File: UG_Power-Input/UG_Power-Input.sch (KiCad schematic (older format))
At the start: 45 parts, among them J1 INPUT, J2 OUTPUT, J3 OUTPUT, U1 LM2679

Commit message: Changes to PCB design
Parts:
- removed H3: 3.5mm, MountingHole:MountingHole_3.5mm, symbol Mechanical:MountingHole
- added H3: 3.5mm, MountingHole:MountingHole_3.5mm_Pad_Via, symbol Mechanical:MountingHole_Pad
- added R3: 0Ω, Resistor_THT:R_Axial_DIN0207_L6.3mm_D2.5mm_P10.16mm_Horizontal, symbol Device:R
- L2, L4: Manufacturer (none) -> Coilcraft
- R2: footprint Resistor_THT:R_Axial_DIN0207_L6.3mm_D2.5mm_P2.54mm_Vertical -> Resistor_THT:R_Axial_DIN0207_L6.3mm_D2.5mm_P10.16mm_Horizontal
- renumbered TP11 to TP10, TP10 to TP11
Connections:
- net -IN: now reaches FL1.2, J1.2 (Pin_2), TP4.1
- net -IN: now also R3.1
- new net: H3.1, R3.2
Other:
- moved on the sheet: C1, C10, C11, C12, C13, C2, C3, C4, C5, C6, C7, C8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

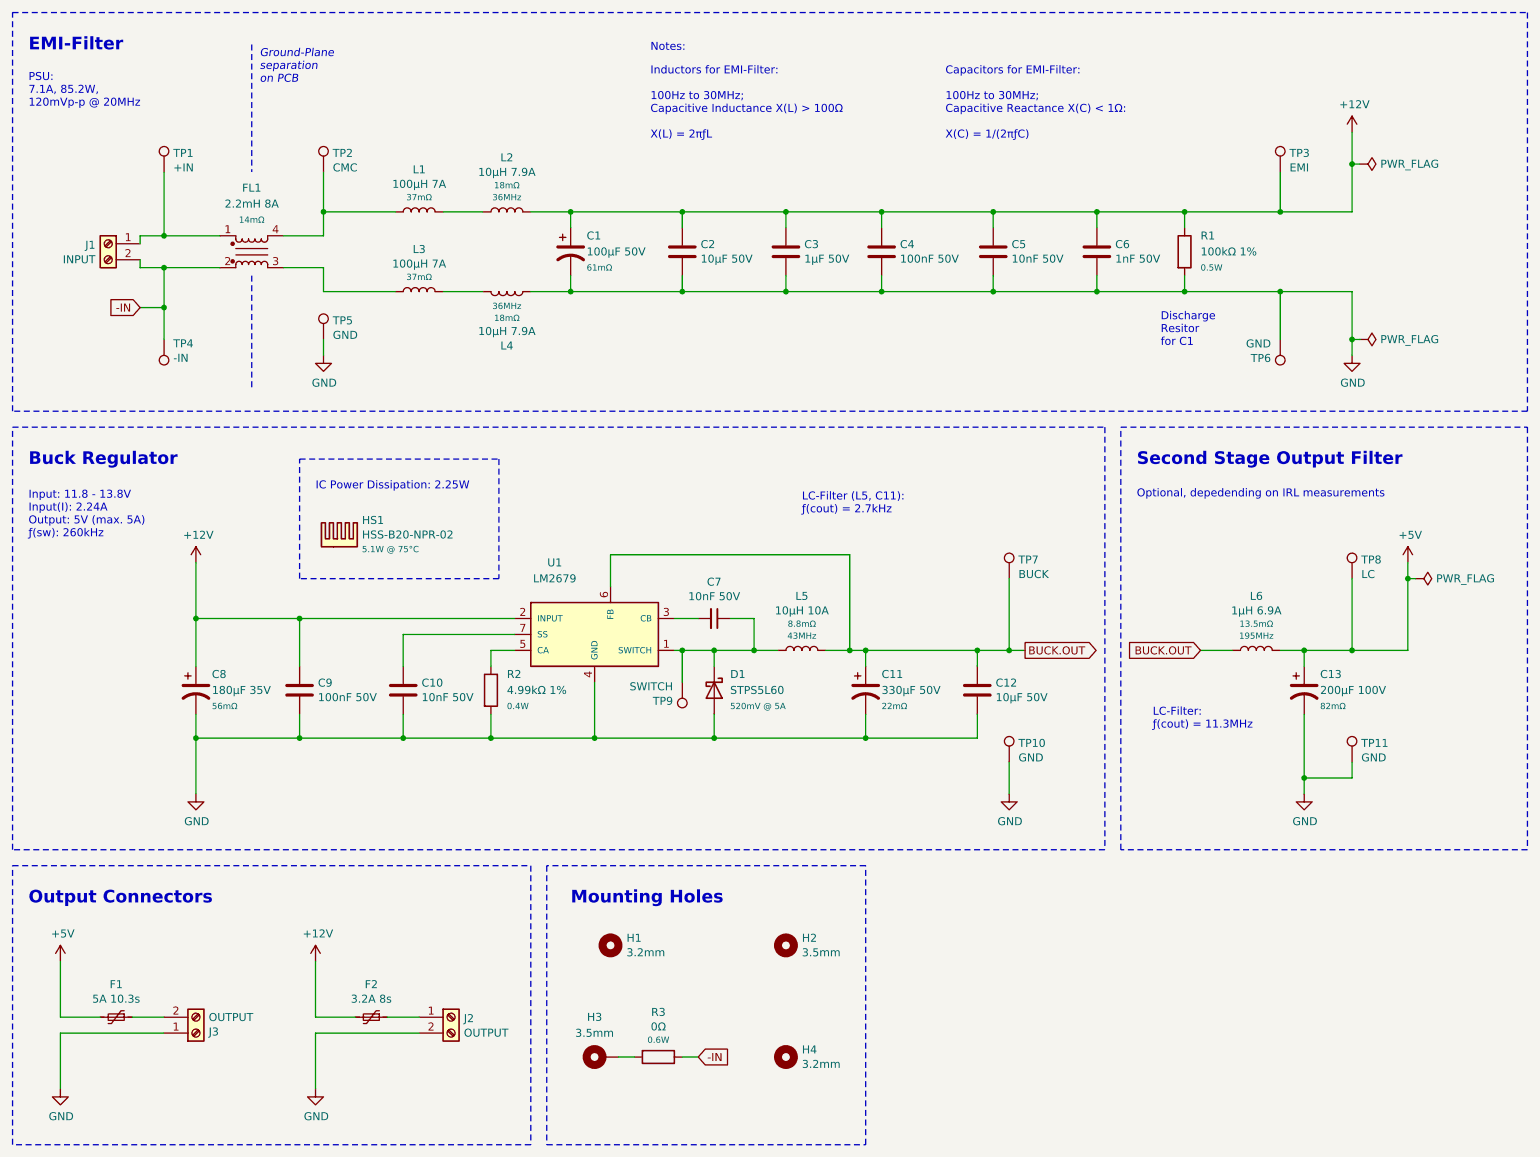
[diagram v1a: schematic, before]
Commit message: Changes to silkscreen on back of PCB
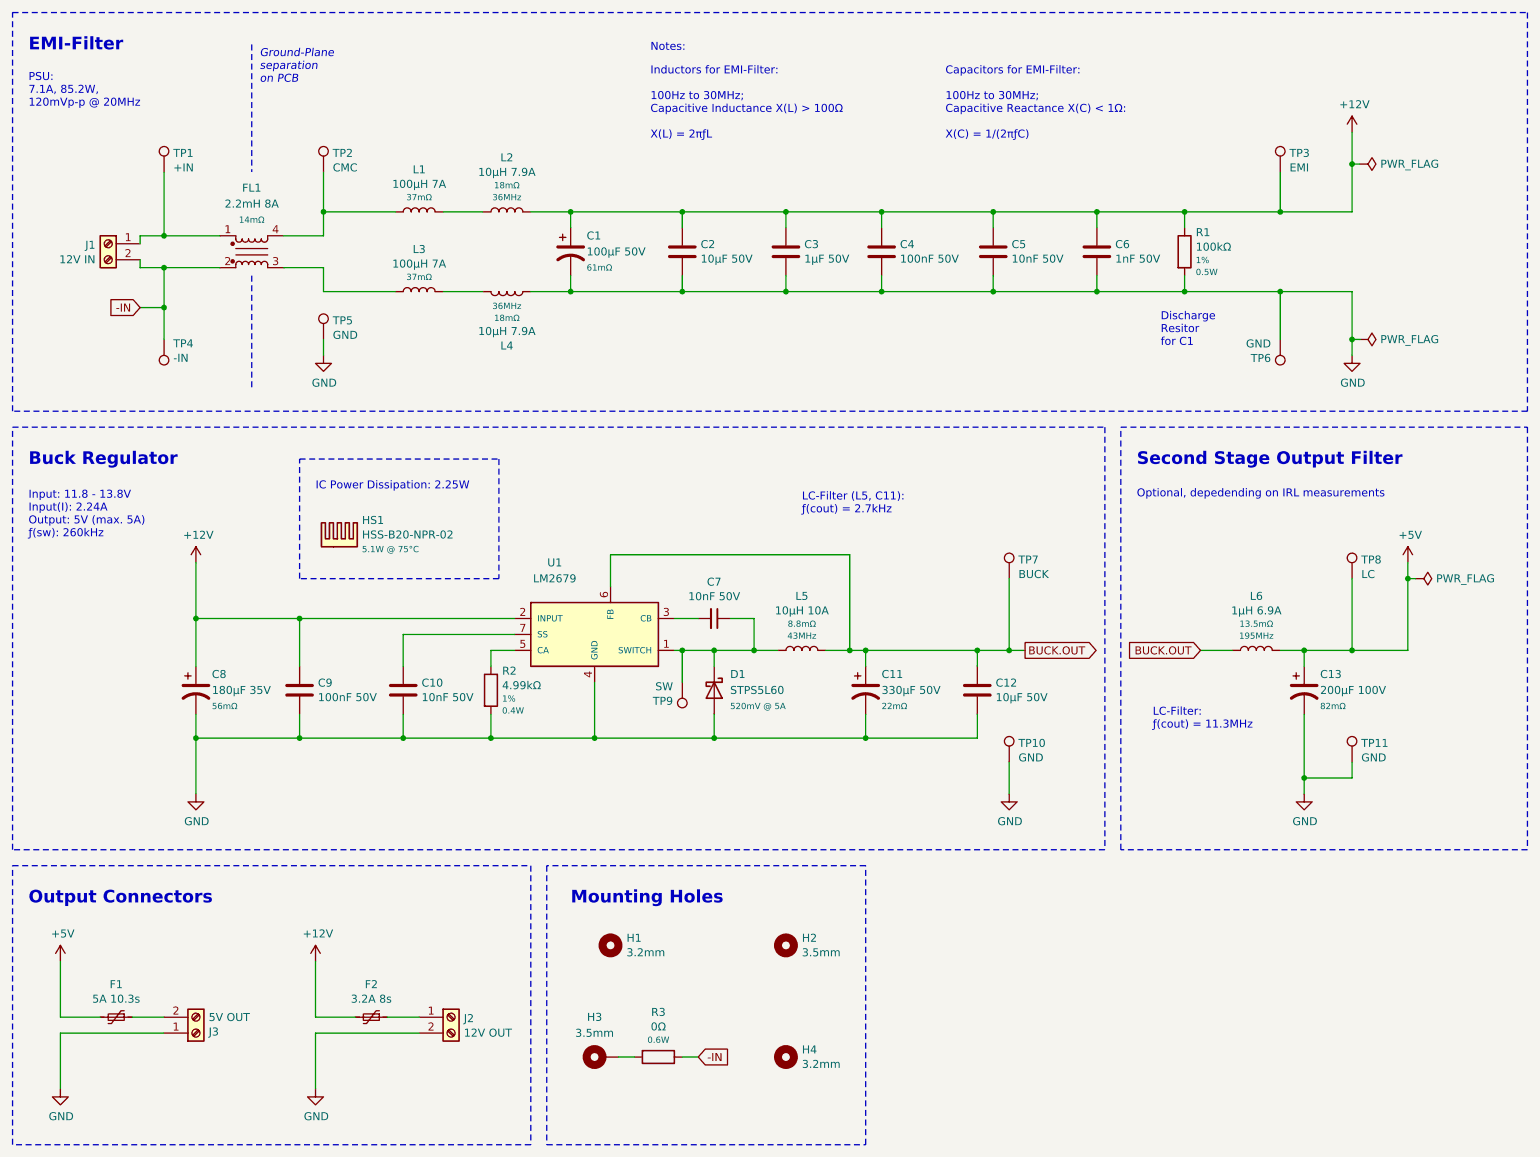
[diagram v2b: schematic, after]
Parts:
- C12: footprint Capacitor_THT:C_MLCC_W5.0mm_L2.5mm_P2.50mm -> Capacitor_THT:C_MLCC_W5.5mm_L4.0mm_P2.50mm
- J1: value INPUT -> 12V IN
- J2: value OUTPUT -> 12V OUT
- J3: value OUTPUT -> 5V OUT
- R1: value 100kΩ 1% -> 100kΩ; Mouser-Nr 594-5053HD100K0F -> (none); Tolerance (none) -> 1%
- R2: value 4.99kΩ 1% -> 4.99kΩ; Mouser-Nr 594-5043ED4K990F -> (none); Tolerance (none) -> 1%
- R3: Tolerance (none) -> 1%
- TP9: value SWITCH -> SW
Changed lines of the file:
@@
 	3200 2350 3650 2350
-$Comp
-L Connector:Screw_Terminal_01x02 J2
-U 1 1 60795962
-P 4000 6900
-AR Path="/60795962" Ref="J2"  Part="1"
-AR Path="/603AD409/60795962" Ref="J?"  Part="1"
-AR Path="/603051B5/60795962" Ref="J?"  Part="1"
-AR Path="/6081FDFC/60795962" Ref="J?"  Part="1"
-AR Path="/6081FDFC/6068D87B/60795962" Ref="J?"  Part="1"
-AR Path="/6081FDFC/60597F98/60795962" Ref="J?"  Part="1"
-AR Path="/60599E1F/605B3C0B/60795962" Ref="J?"  Part="1"
-F 0 "J2" H 4080 6892 50  0000 L CNN
-F 1 "OUTPUT" H 4080 6801 50  0000 L CNN
-F 2 "TerminalBlock_Phoenix:TerminalBlock_Phoenix_MKDS-1,5-2-5.08_1x02_P5.08mm_Horizontal" H 4000 6900 50  0001 C CNN
-F 3 "" H 4000 6900 50  0001 C CNN
-F 4 "" H 4000 6900 50  0001 C CNN "Manufacturer"
-F 5 "" H 4000 6900 50  0001 C CNN "Part-Nr."
-F 6 "~" H 4000 6900 50  0001 C CNN "Mouser-Nr"
-	1    4000 6900
-	1    0    0    -1
-$EndComp
 $Comp
 L power:GND #PWR011
@@
 AR Path="/60599E1F/605B3C0B/60791571" Ref="J?"  Part="1"
 F 0 "J3" H 2480 6992 50  0000 L CNN
-F 1 "OUTPUT" H 2480 6901 50  0000 L CNN
+F 1 "5V OUT" H 2480 6901 50  0000 L CNN
 F 2 "TerminalBlock_Phoenix:TerminalBlock_Phoenix_MKDS-1,5-2-5.08_1x02_P5.08mm_Horizontal" H 2400 7000 50  0001 C CNN
 F 3 "" H 2400 7000 50  0001 C CNN
@@
 $EndComp
 $Comp
-L Device:R R1
-U 1 1 606CFBD5
-P 8600 2100
-F 0 "R1" H 8700 2200 50  0000 L CNN
-F 1 "100kΩ 1%" H 8700 2100 50  0000 L CNN
-F 2 "Resistor_THT:R_Axial_DIN0207_L6.3mm_D2.5mm_P10.16mm_Horizontal" V 8530 2100 50  0001 C CNN
-F 3 "https://www.vishay.com/docs/28722/sfr16s25.pdf" H 8600 2100 50  0001 C CNN
-F 4 "Vishay" H 8600 2100 50  0001 C CNN "Manufacturer"
-F 5 "SFR25H0001003FR500" H 8600 2100 50  0001 C CNN "Part-Nr."
-F 6 "594-5053HD100K0F" H 8600 2100 50  0001 C CNN "Mouser-Nr"
-F 7 "0.5W" H 8700 2000 39  0000 L CNN "Power"
-	1    8600 2100
-	1    0    0    -1
-$EndComp
-$Comp
 L Device:CP1 C1
 U 1 1 6063D390
@@
 Wire Wire Line
 	2050 2000 2050 2050
-$Comp
-L Connector:Screw_Terminal_01x02 J1
-U 1 1 606A0DCB
-P 1850 2050
-AR Path="/606A0DCB" Ref="J1"  Part="1"
-AR Path="/603AD409/606A0DCB" Ref="J?"  Part="1"
-AR Path="/603051B5/606A0DCB" Ref="J?"  Part="1"
-AR Path="/6081FDFC/606A0DCB" Ref="J?"  Part="1"
-AR Path="/6081FDFC/6068D87B/606A0DCB" Ref="J?"  Part="1"
-AR Path="/6081FDFC/60597F98/606A0DCB" Ref="J?"  Part="1"
-AR Path="/60599E1F/605B3C0B/606A0DCB" Ref="J?"  Part="1"
-F 0 "J1" H 1930 2042 50  0000 L CNN
-F 1 "INPUT" H 1930 1951 50  0000 L CNN
-F 2 "TerminalBlock_Phoenix:TerminalBlock_Phoenix_MKDS-1,5-2-5.08_1x02_P5.08mm_Horizontal" H 1850 2050 50  0001 C CNN
-F 3 "" H 1850 2050 50  0001 C CNN
-F 4 "" H 1850 2050 50  0001 C CNN "Manufacturer"
-F 5 "" H 1850 2050 50  0001 C CNN "Part-Nr."
-F 6 "~" H 1850 2050 50  0001 C CNN "Mouser-Nr"
-	1    1850 2050
-	-1   0    0    -1
-$EndComp
 Connection ~ 2200 2000
 Wire Wire Line
@@
 	4250 4600 4250 4700
 $Comp
-L Device:R R2
-U 1 1 607065A9
-P 4250 4850
-F 0 "R2" H 4350 4950 50  0000 L CNN
-F 1 "4.99kΩ 1%" H 4350 4850 50  0000 L CNN
-F 2 "Resistor_THT:R_Axial_DIN0207_L6.3mm_D2.5mm_P10.16mm_Horizontal" V 4180 4850 50  0001 C CNN
-F 3 "https://www.vishay.com/docs/28722/sfr16s25.pdf" H 4250 4850 50  0001 C CNN
-F 4 "Vishay" H 4250 4850 50  0001 C CNN "Manufacturer"
-F 5 "594-5043ED4K990F" H 4250 4850 50  0001 C CNN "Mouser-Nr"
-F 6 "SFR2500004991FR500" H 4250 4850 50  0001 C CNN "Part-Nr."
-F 7 "0.4W" H 4350 4750 39  0000 L CNN "Power"
-	1    4250 4850
-	1    0    0    -1
-$EndComp
-$Comp
 L power:GND #PWR02
 U 1 1 60B1443E
@@
 P 5450 4800
 F 0 "TP9" H 5508 4918 50  0000 L CNN
-F 1 "SWITCH" H 5508 4827 50  0000 L CNN
+F 1 "SW" H 5508 4827 50  0000 L CNN
 F 2 "TestPoint:TestPoint_Keystone_5000-5004_Miniature" H 5650 4800 50  0001 C CNN
 F 3 "https://www.keyelco.com/userAssets/file/M65p56.pdf" H 5650 4800 50  0001 C CNN
@@
 F 0 "C12" H 7415 4896 50  0000 L CNN
 F 1 "10µF 50V" H 7415 4805 50  0000 L CNN
-F 2 "Capacitor_THT:C_MLCC_W5.0mm_L2.5mm_P2.50mm" H 7338 4700 50  0001 C CNN
+F 2 "Capacitor_THT:C_MLCC_W5.5mm_L4.0mm_P2.50mm" H 7338 4700 50  0001 C CNN
 F 3 "https://search.murata.co.jp/Ceramy/image/img/A01X/G101/ENG/RDE_X7R_X7S_25V-100V_E.pdf" H 7300 4850 50  0001 C CNN
 F 4 "Murata" H 7300 4850 50  0001 C CNN "Manufacturer"
@@
 Text GLabel 5550 7150 2    50   Input ~ 0
 -IN
+Wire Wire Line
+	5050 7150 5150 7150
+Wire Wire Line
+	5450 7150 5550 7150
+$Comp
+L Device:R R1
+U 1 1 6099B107
+P 8600 2100
+F 0 "R1" H 8670 2221 50  0000 L CNN
+F 1 "100kΩ" H 8670 2130 50  0000 L CNN
+F 2 "Resistor_THT:R_Axial_DIN0207_L6.3mm_D2.5mm_P10.16mm_Horizontal" V 8530 2100 50  0001 C CNN
+F 3 "https://www.vishay.com/docs/28722/sfr16s25.pdf" H 8600 2100 50  0001 C CNN
+F 4 "1%" H 8670 2047 39  0000 L CNN "Tolerance"
+F 5 "0.5W" H 8670 1972 39  0000 L CNN "Power"
+F 6 "Vishay" H 8600 2100 50  0001 C CNN "Manufacturer"
+F 7 "SFR25H0001003FR500" H 8600 2100 50  0001 C CNN "Part-Nr."
+	1    8600 2100
+	1    0    0    -1
+$EndComp
+$Comp
+L Device:R R2
+U 1 1 6099F974
+P 4250 4850
+F 0 "R2" H 4320 4971 50  0000 L CNN
+F 1 "4.99kΩ" H 4320 4880 50  0000 L CNN
+F 2 "Resistor_THT:R_Axial_DIN0207_L6.3mm_D2.5mm_P10.16mm_Horizontal" V 4180 4850 50  0001 C CNN
+F 3 "https://www.vishay.com/docs/28722/sfr16s25.pdf" H 4250 4850 50  0001 C CNN
+F 4 "1%" H 4320 4797 39  0000 L CNN "Tolerance"
+F 5 "0.4W" H 4320 4722 39  0000 L CNN "Power"
+F 6 "Vishay" H 4250 4850 50  0001 C CNN "Manufacturer"
+F 7 "SFR2500004991FR500" H 4250 4850 50  0001 C CNN "Part-Nr."
+	1    4250 4850
+	1    0    0    -1
+$EndComp
 $Comp
 L Device:R R3
-U 1 1 60899817
+U 1 1 609A09E8
 P 5300 7150
 F 0 "R3" V 5019 7150 50  0000 C CNN
@@
 F 2 "Resistor_THT:R_Axial_DIN0207_L6.3mm_D2.5mm_P10.16mm_Horizontal" V 5230 7150 50  0001 C CNN
 F 3 "https://www.vishay.com/docs/28766/mbxsma.pdf" H 5300 7150 50  0001 C CNN
-F 4 "Vishay" H 5300 7150 50  0001 C CNN "Manufacturer"
-F 5 "MBB02070Z0000ZCT00" H 5300 7150 50  0001 C CNN "Part-Nr."
-F 6 "0.6W" V 5193 7150 39  0000 C CNN "Power"
+F 4 "1%" V 5117 7150 39  0001 C CNN "Tolerance"
+F 5 "0.6W" V 5193 7150 39  0000 C CNN "Power"
+F 6 "Vishay" H 5300 7150 50  0001 C CNN "Manufacturer"
+F 7 "MBB02070Z0000ZCT00" H 5300 7150 50  0001 C CNN "Part-Nr."
 	1    5300 7150
 	0    1    1    0
 $EndComp
-Wire Wire Line
-	5050 7150 5150 7150
-Wire Wire Line
-	5450 7150 5550 7150
+$Comp
+L Connector:Screw_Terminal_01x02 J1
+U 1 1 606A0DCB
+P 1850 2050
+AR Path="/606A0DCB" Ref="J1"  Part="1"
+AR Path="/603AD409/606A0DCB" Ref="J?"  Part="1"
+AR Path="/603051B5/606A0DCB" Ref="J?"  Part="1"
+AR Path="/6081FDFC/606A0DCB" Ref="J?"  Part="1"
+AR Path="/6081FDFC/6068D87B/606A0DCB" Ref="J?"  Part="1"
+AR Path="/6081FDFC/60597F98/606A0DCB" Ref="J?"  Part="1"
+AR Path="/60599E1F/605B3C0B/606A0DCB" Ref="J?"  Part="1"
+F 0 "J1" H 1930 2042 50  0000 L CNN
+F 1 "12V IN" H 1930 1951 50  0000 L CNN
+F 2 "TerminalBlock_Phoenix:TerminalBlock_Phoenix_MKDS-1,5-2-5.08_1x02_P5.08mm_Horizontal" H 1850 2050 50  0001 C CNN
+F 3 "" H 1850 2050 50  0001 C CNN
+F 4 "" H 1850 2050 50  0001 C CNN "Manufacturer"
+F 5 "" H 1850 2050 50  0001 C CNN "Part-Nr."
+F 6 "~" H 1850 2050 50  0001 C CNN "Mouser-Nr"
+	1    1850 2050
+	-1   0    0    -1
+$EndComp
+$Comp
+L Connector:Screw_Terminal_01x02 J2
+U 1 1 60795962
+P 4000 6900
+AR Path="/60795962" Ref="J2"  Part="1"
+AR Path="/603AD409/60795962" Ref="J?"  Part="1"
+AR Path="/603051B5/60795962" Ref="J?"  Part="1"
+AR Path="/6081FDFC/60795962" Ref="J?"  Part="1"
+AR Path="/6081FDFC/6068D87B/60795962" Ref="J?"  Part="1"
+AR Path="/6081FDFC/60597F98/60795962" Ref="J?"  Part="1"
+AR Path="/60599E1F/605B3C0B/60795962" Ref="J?"  Part="1"
+F 0 "J2" H 4080 6892 50  0000 L CNN
+F 1 "12V OUT" H 4080 6801 50  0000 L CNN
+F 2 "TerminalBlock_Phoenix:TerminalBlock_Phoenix_MKDS-1,5-2-5.08_1x02_P5.08mm_Horizontal" H 4000 6900 50  0001 C CNN
+F 3 "" H 4000 6900 50  0001 C CNN
+F 4 "" H 4000 6900 50  0001 C CNN "Manufacturer"
+F 5 "" H 4000 6900 50  0001 C CNN "Part-Nr."
+F 6 "~" H 4000 6900 50  0001 C CNN "Mouser-Nr"
+	1    4000 6900
+	1    0    0    -1
+$EndComp
 $EndSCHEMATC

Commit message: Changes to schematic values, footprints on PCB, BOM
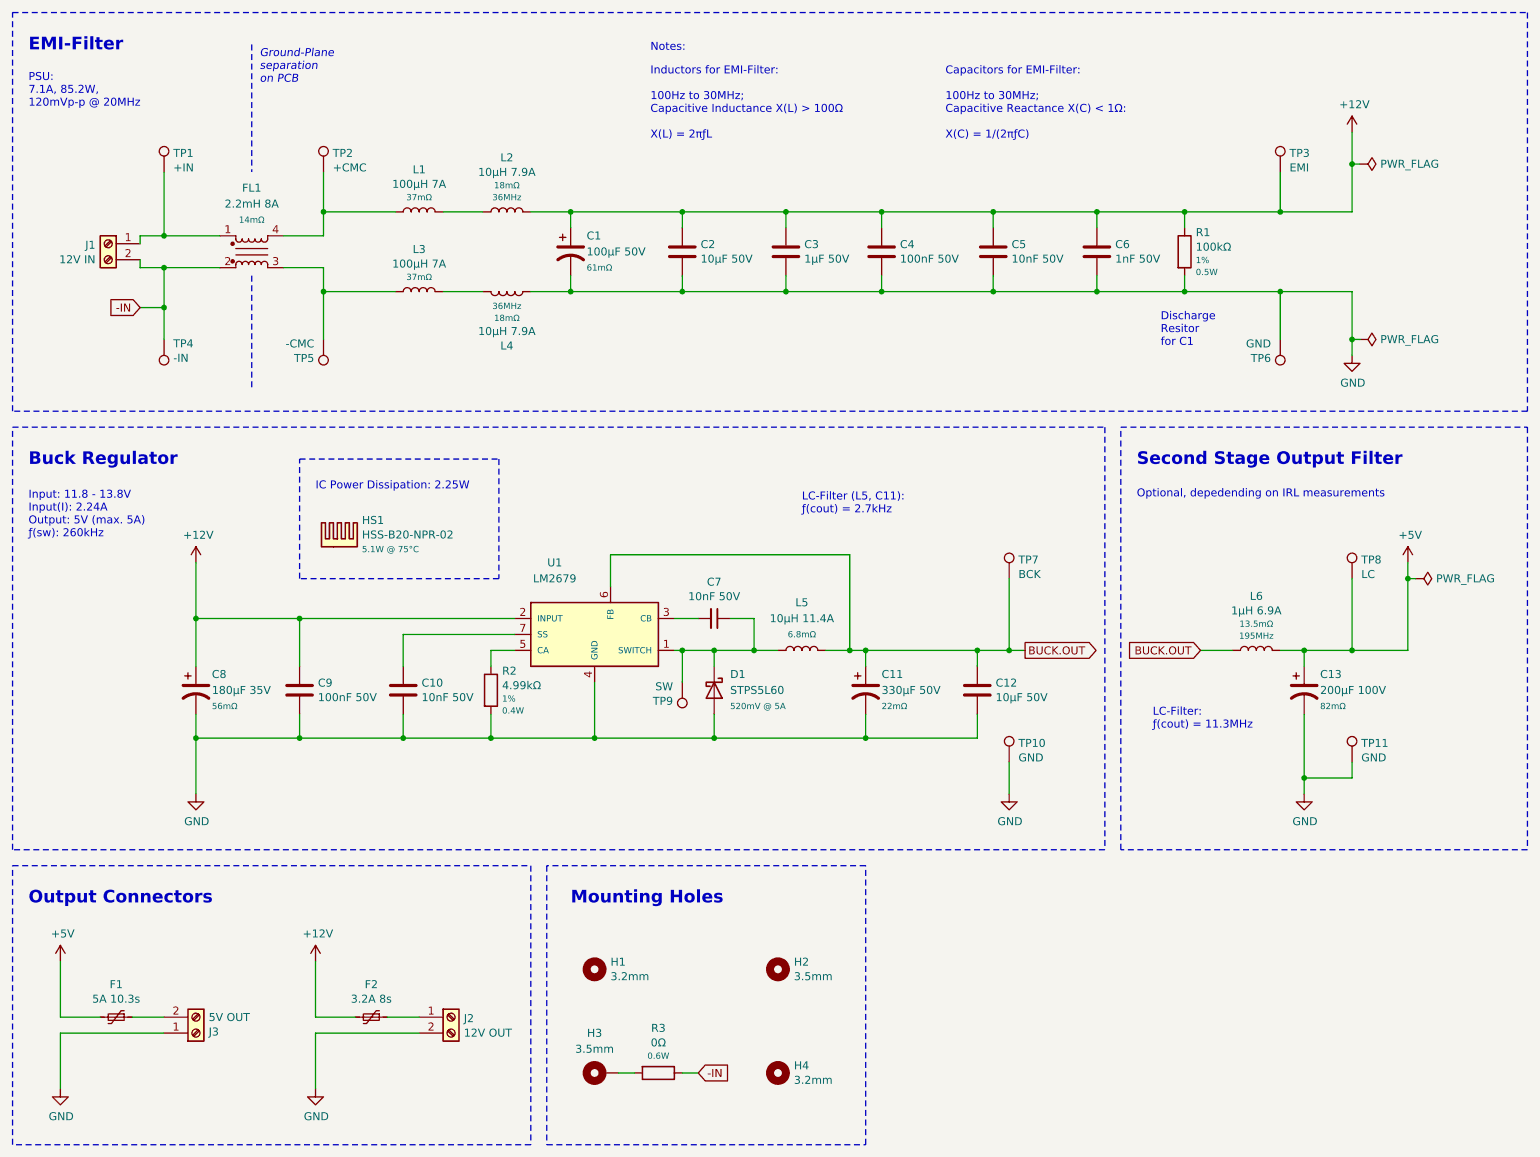
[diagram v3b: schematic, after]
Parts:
- C12: Part-Nr. RDER71H103K0S1H03A -> RDEC71H106K3S1H03A
- L2, L4: Part-Nr. (none) -> RFS1412-103ME; Tolerance (none) -> 20%
- L5: value 10µH 10A -> 10µH 11.4A; DCR 8.8mΩ -> 6.8mΩ; Part-Nr. 744711010 -> 744750560100; SRF 43MHz -> MHz
- TP2: value CMC -> +CMC
- TP5: value GND -> -CMC
- TP7: value BUCK -> BCK
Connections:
- net GND: no longer TP5.1
- net at FL1.3, L3.1: now also TP5.1
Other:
- moved on the sheet: H1, H2, H3, H4, R3, TP5

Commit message: Changes to PCB & BOM
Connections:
- net GND: now also J3.2 (Pin_2); no longer J3.1 (Pin_1)
- net at F1.1: now also J3.1 (Pin_1); no longer J3.2 (Pin_2)
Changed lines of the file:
@@
 L Connector:Screw_Terminal_01x02 J3
 U 1 1 60791571
-P 2400 7000
+P 2400 6900
 AR Path="/60791571" Ref="J3"  Part="1"
 AR Path="/603AD409/60791571" Ref="J?"  Part="1"
@@
 AR Path="/6081FDFC/60597F98/60791571" Ref="J?"  Part="1"
 AR Path="/60599E1F/605B3C0B/60791571" Ref="J?"  Part="1"
-F 0 "J3" H 2480 6992 50  0000 L CNN
-F 1 "5V OUT" H 2480 6901 50  0000 L CNN
-F 2 "TerminalBlock_Phoenix:TerminalBlock_Phoenix_MKDS-1,5-2-5.08_1x02_P5.08mm_Horizontal" H 2400 7000 50  0001 C CNN
-F 3 "" H 2400 7000 50  0001 C CNN
-F 4 "" H 2400 7000 50  0001 C CNN "Manufacturer"
-F 5 "" H 2400 7000 50  0001 C CNN "Part-Nr."
-F 6 "~" H 2400 7000 50  0001 C CNN "Mouser-Nr"
-	1    2400 7000
-	1    0    0    1
+F 0 "J3" H 2480 6892 50  0000 L CNN
+F 1 "5V OUT" H 2480 6801 50  0000 L CNN
+F 2 "TerminalBlock_Phoenix:TerminalBlock_Phoenix_MKDS-1,5-2-5.08_1x02_P5.08mm_Horizontal" H 2400 6900 50  0001 C CNN
+F 3 "" H 2400 6900 50  0001 C CNN
+F 4 "" H 2400 6900 50  0001 C CNN "Manufacturer"
+F 5 "" H 2400 6900 50  0001 C CNN "Part-Nr."
+F 6 "~" H 2400 6900 50  0001 C CNN "Mouser-Nr"
+	1    2400 6900
+	1    0    0    -1
 $EndComp
 $Comp
